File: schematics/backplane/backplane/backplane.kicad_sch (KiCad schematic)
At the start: 24 parts, among them IC3 SN74LV4052ADBR, J10 Conn_ARM_JTAG_SWD_10, J11 UART RS232, J12 Pins, SW1 Reset, U1 STM32F303RETx, Y1 8-25 MHz, Y2 32....khz

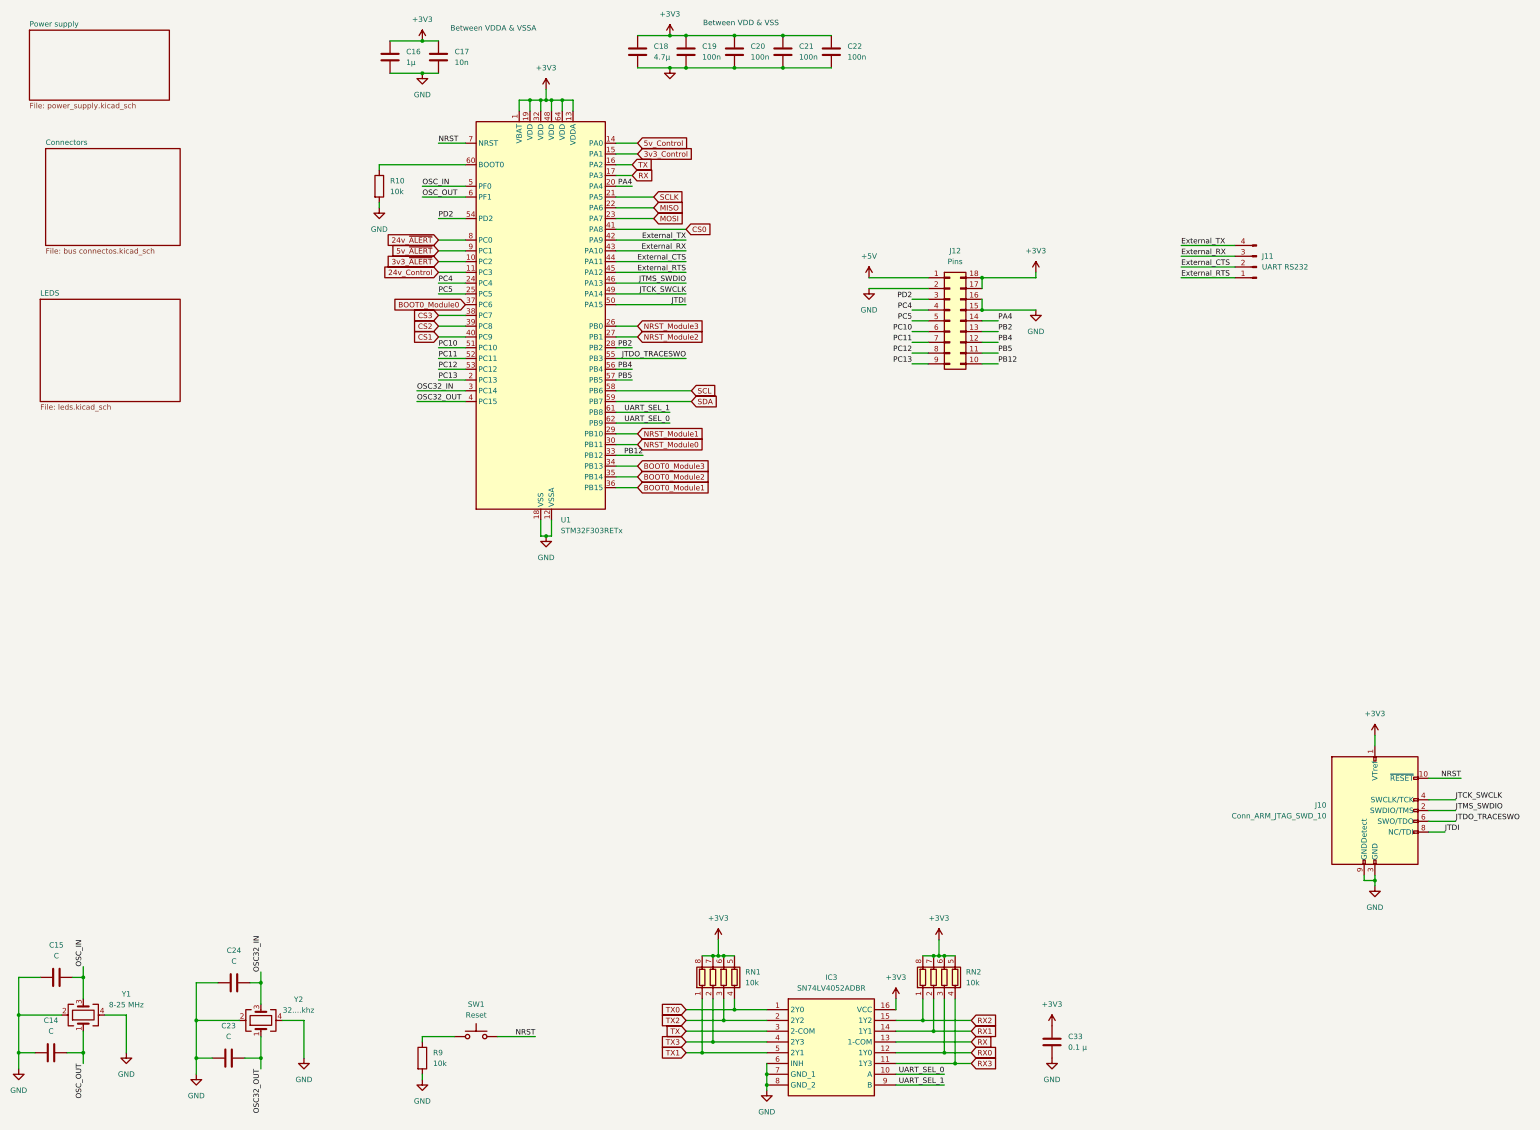
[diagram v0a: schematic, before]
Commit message: Add crystal data and Test points
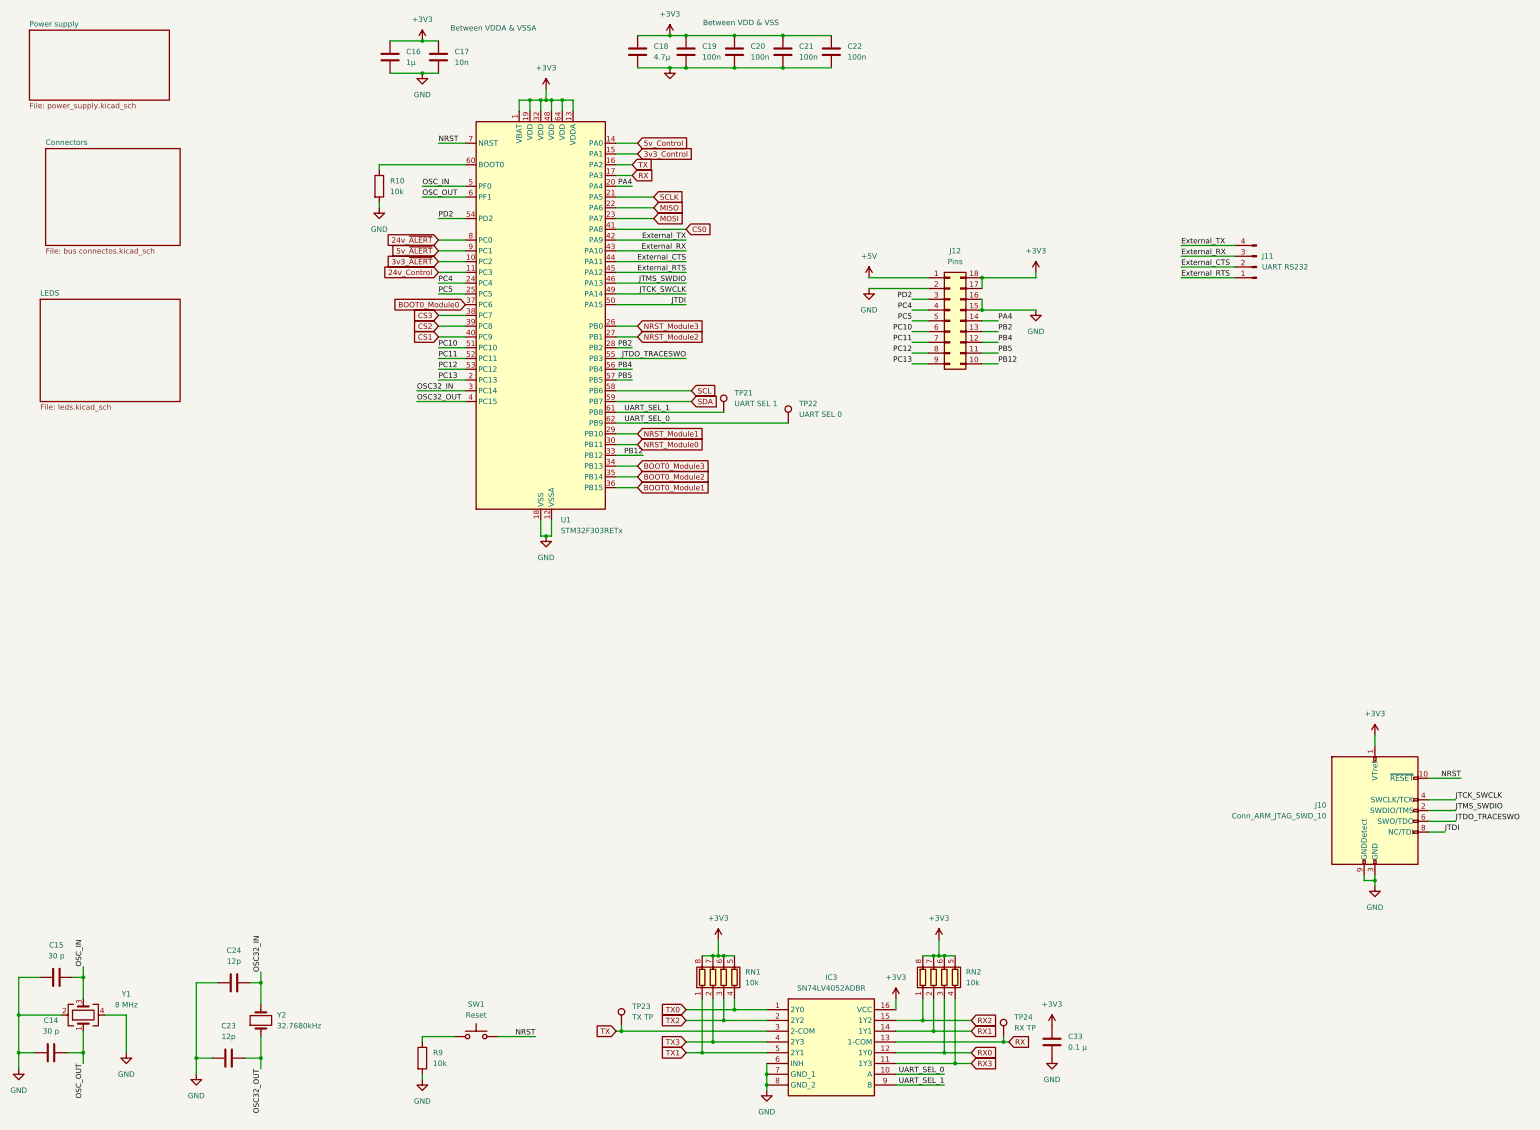
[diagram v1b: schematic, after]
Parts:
- removed Y2: 32....khz, symbol Device:Crystal_GND24
- added TP21: UART SEL 1, TestPoint:TestPoint_Keystone_5000-5004_Miniature, symbol Connector:TestPoint
- added TP22: UART SEL 0, TestPoint:TestPoint_Keystone_5000-5004_Miniature, symbol Connector:TestPoint
- added TP23: TX TP, TestPoint:TestPoint_Keystone_5000-5004_Miniature, symbol Connector:TestPoint
- added TP24: RX TP, TestPoint:TestPoint_Keystone_5000-5004_Miniature, symbol Connector:TestPoint
- added Y2: 32.7680kHz, Crystal:Crystal_SMD_2012-2Pin_2.0x1.2mm_HandSoldering, symbol Device:Crystal
- C14, C15: value C -> 30 p
- C23, C24: value C -> 12p
- Y1: value 8-25 MHz -> 8 MHz; footprint (none) -> custom:WE-XTAL_CFPX-104
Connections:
- net OSC32_IN: now also Y2.2
- net OSC32_OUT: now also Y2.1
- net RX: now also TP24.1
- net TX: now also TP23.1
- net UART_SEL_0: now also TP22.1
- net UART_SEL_1: now also TP21.1
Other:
- title: (none) -> OpenMTB

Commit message: redo numbering
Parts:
- renumbered C18 to C1, C24 to C10, C23 to C11, C33 to C12, C19 to C2, C20 to C3, C21 to C4, C22 to C5, C16 to C6, C17 to C7, C15 to C8, C14 to C9, IC3 to IC1, J10 to J1, J12 to J2, J11 to J3, R9 to R1, R10 to R39, TP23 to TP1, TP24 to TP2, TP21 to TP23, TP22 to TP24
